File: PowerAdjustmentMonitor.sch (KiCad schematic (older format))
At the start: 19 parts

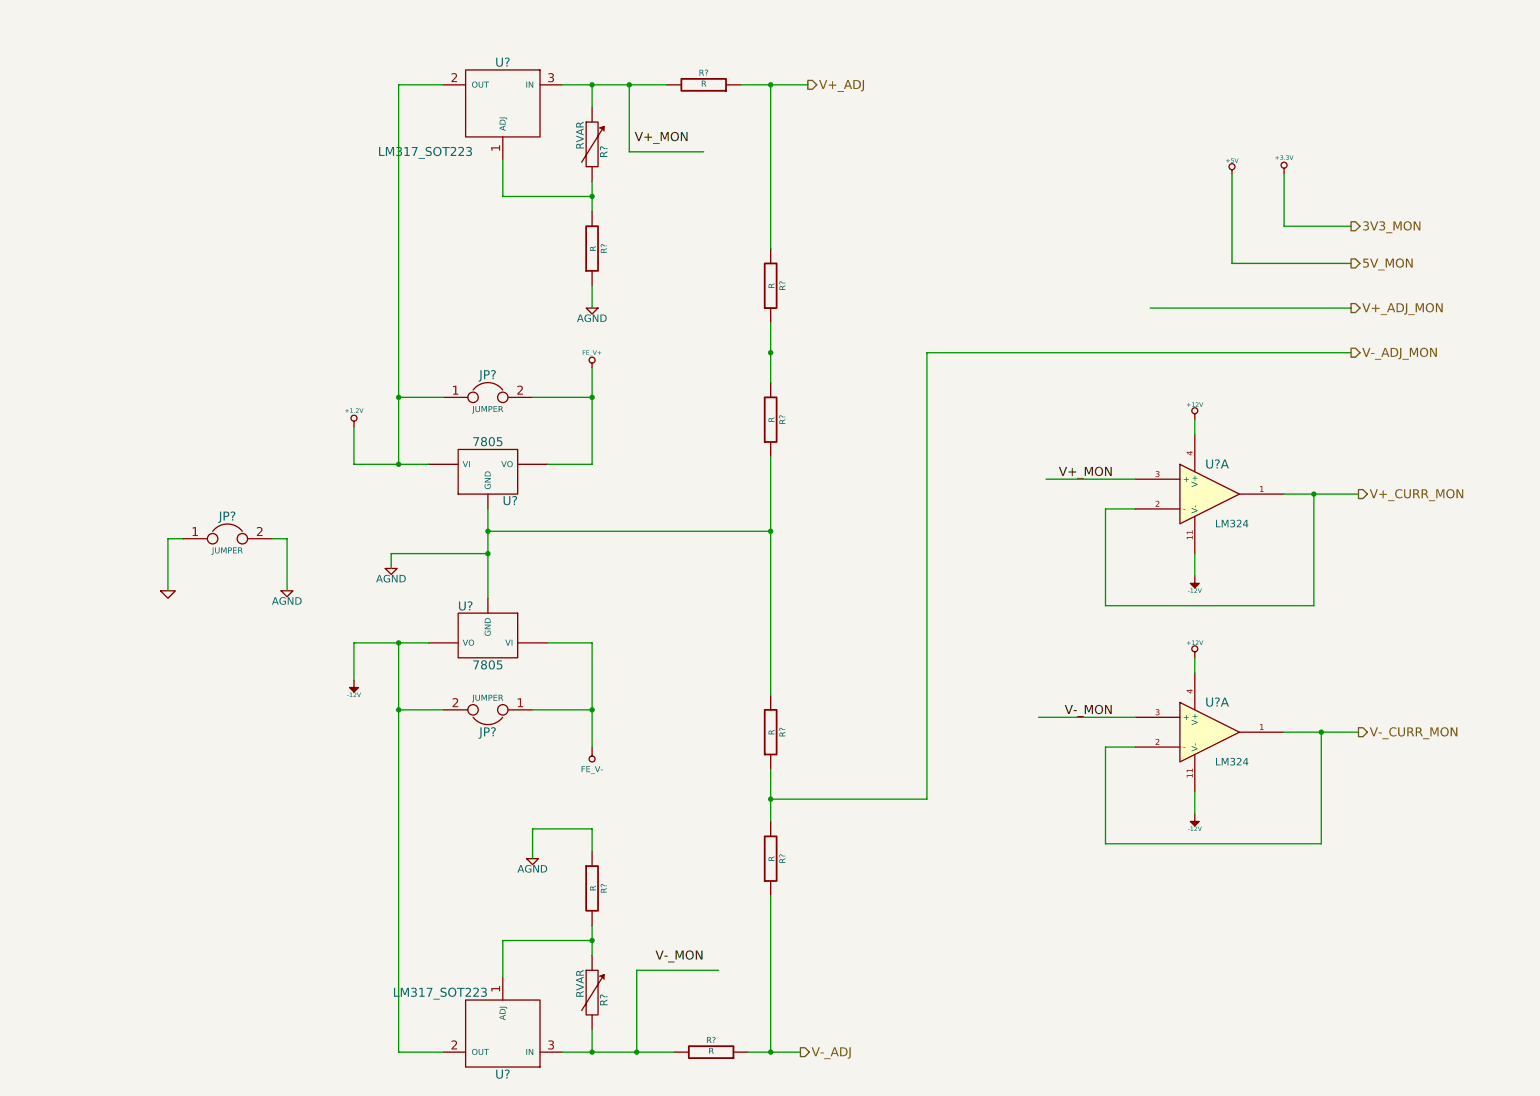
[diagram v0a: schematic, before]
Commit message: Added Relay module footprints.
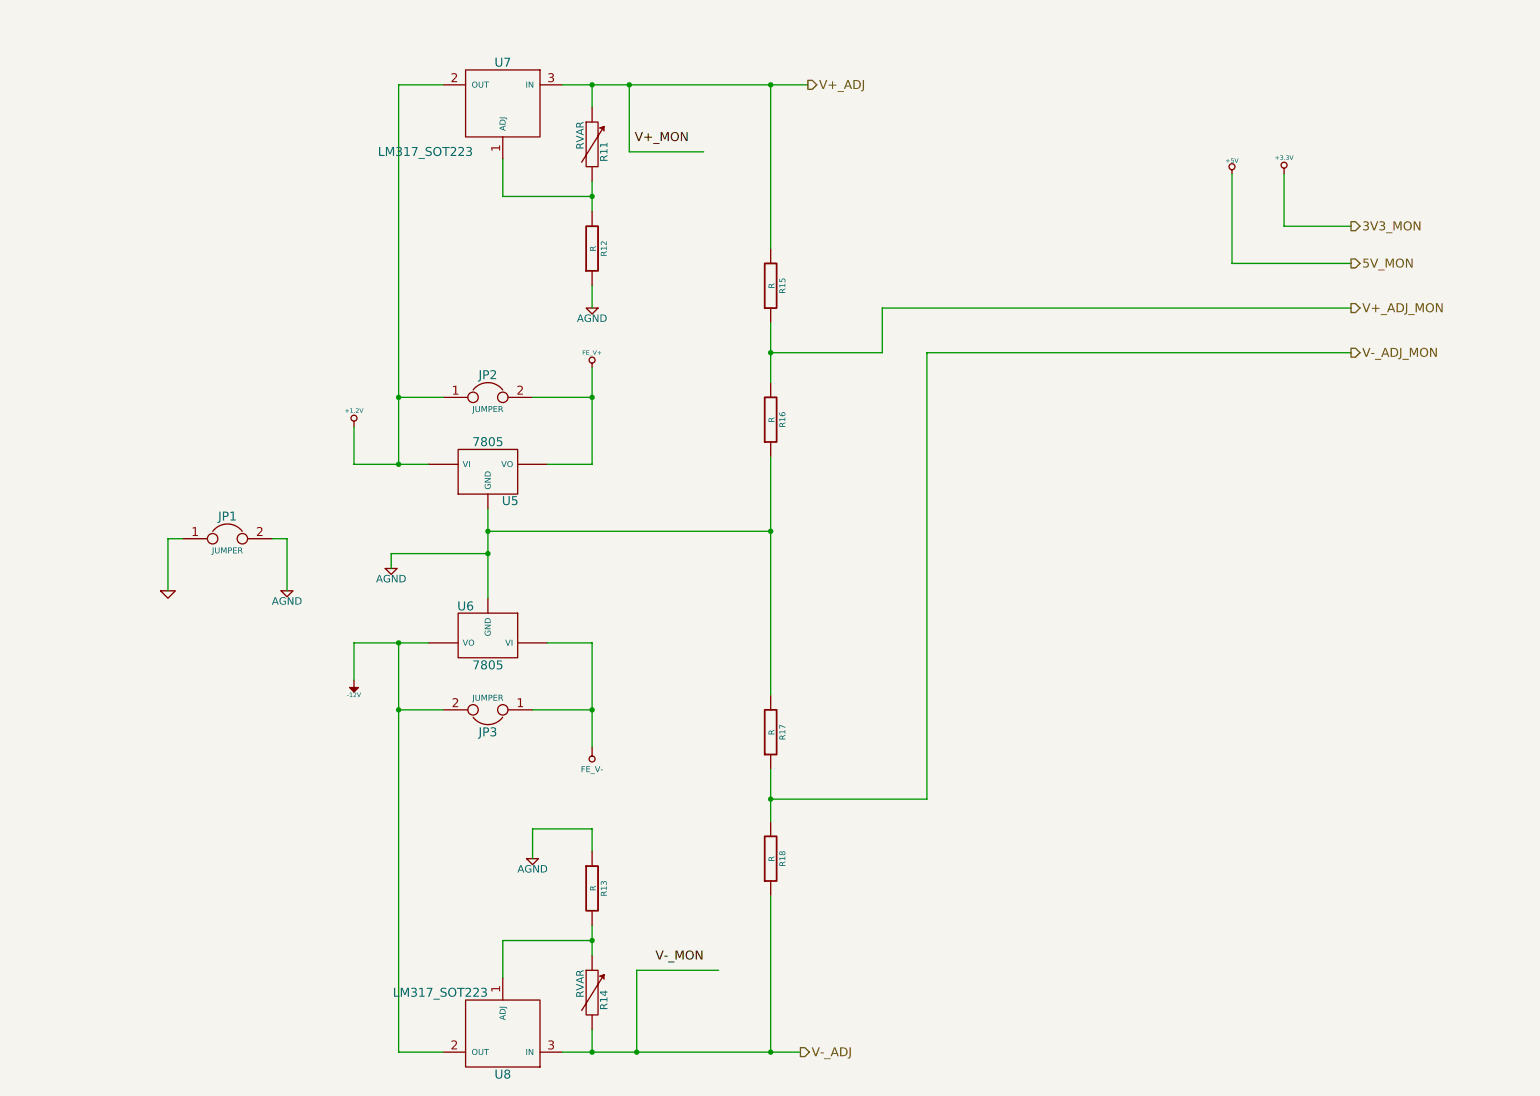
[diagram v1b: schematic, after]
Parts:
- removed R? (x2): R, symbol R
- removed U? (x2): LM324, symbol LM324
- gave numbers to parts that had none: 15
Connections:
- net labels removed: +12V, V+_CURR_MON, V-_CURR_MON
- wire segments 94 -> 57

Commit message: Associated and placed thermocouple, terminal, arduino, fan driver, power protection modules.
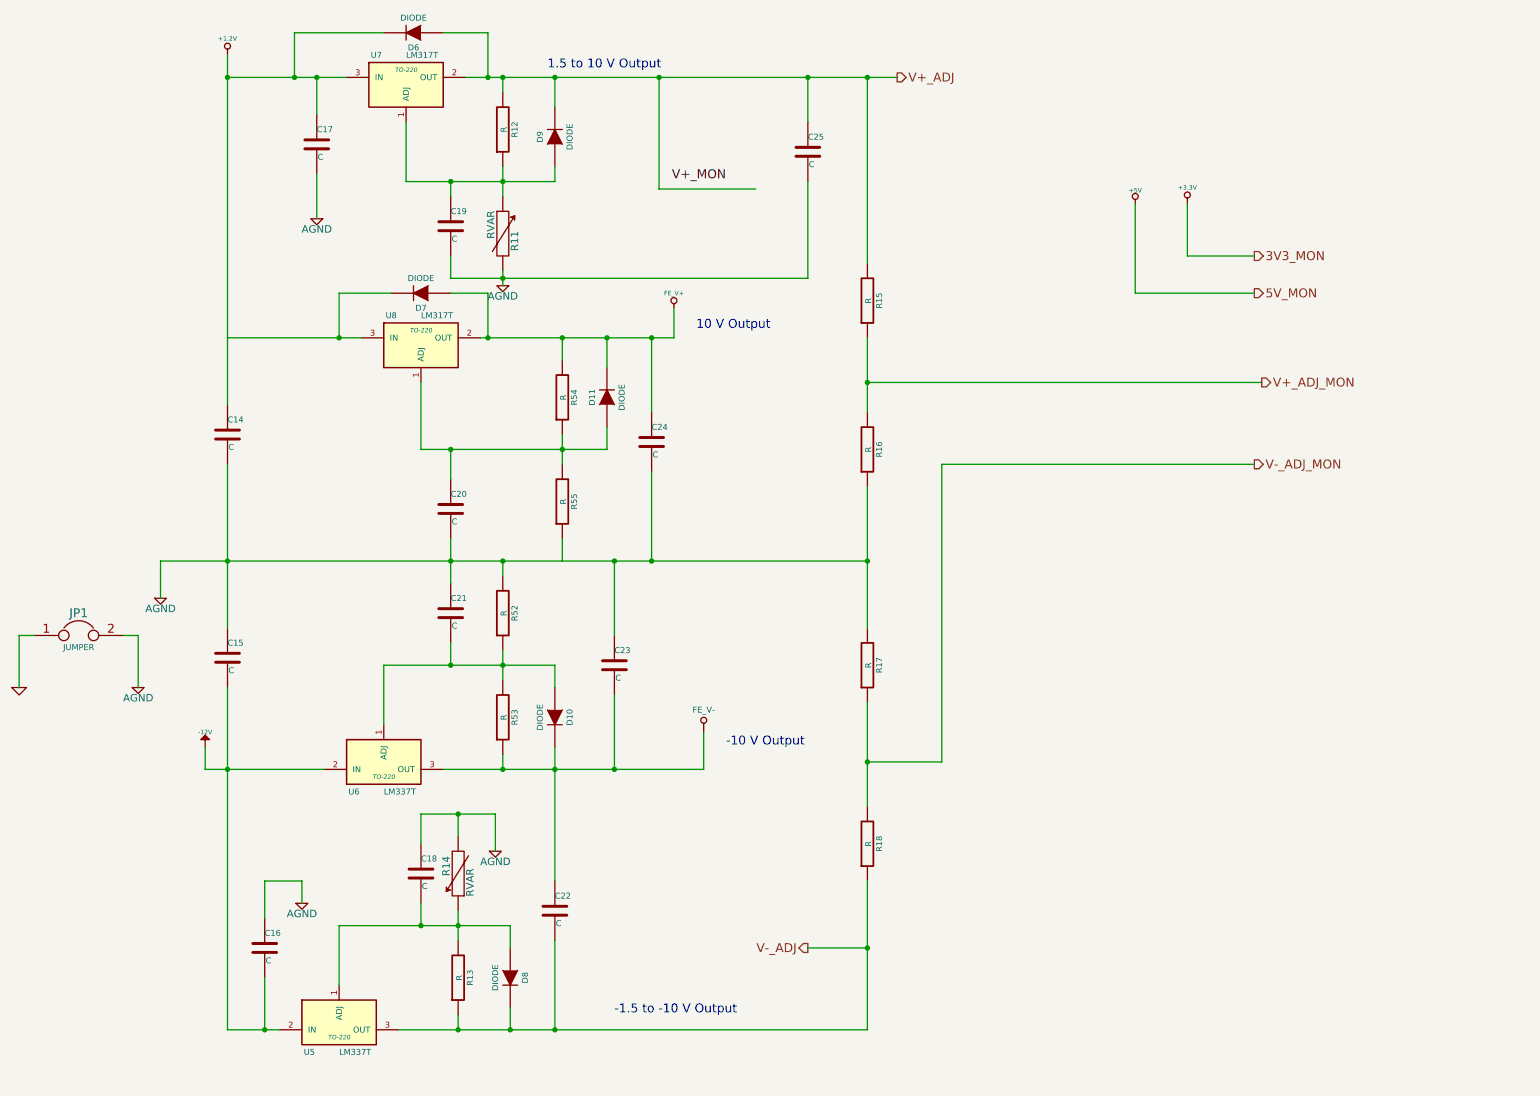
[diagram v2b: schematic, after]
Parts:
- removed JP2, JP3: JUMPER, symbol JUMPER
- removed U5, U6: 7805, symbol 7805
- removed U7, U8: LM317_SOT223, symbol LM317_SOT223
- added C14, C15, C16, C17, C18, C19, C20, C21, C22, C23, C24, C25: C, symbol C
- added D10, D11, D6, D7, D8, D9: DIODE, symbol DIODE
- added R52, R53, R54, R55: R, symbol R
- added U5, U6: LM337T, TO-220, symbol LM337T
- added U7, U8: LM317T, TO-220, symbol LM317T
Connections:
- net labels removed: V-_MON
- wire segments 57 -> 95
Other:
- note added: "-1.5 to -10 V Output"
- note added: "-10 V Output"
- note added: "1.5 to 10 V Output"
- note added: "10 V Output"
- moved on the sheet: JP1, R11, R12, R15, R16, R17, R18

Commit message: Layout sessions 1-4.
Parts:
- removed JP1: JUMPER, symbol JUMPER
- removed U7, U8: LM317T, TO-220, symbol LM317T
- added D12, D13: MMBD914-7-F, symbol DIODE
- added U7, U8: LM317_BB, TO-220, symbol LM317_BB
- D10, D11, D6, D7, D8: value DIODE -> MMBD914-7-F; MFG Part Number (none) -> MMBD914-7-F; MFG name (none) -> Diodes Inc
- D9: value DIODE -> MMBD914-7-F; MFG Part Number (none) -> MMBD914-7-F; MFG name (none) -> DiodeS Inc
- R11, R14: value RVAR -> 5K
- R12, R13: value R -> 715
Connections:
- net +1.2V: now also U7.2 (IN)
- net -12V: now also D12.2 (K), D13.2 (K)
- net AGND: now also D10.2 (K), R55.1; no longer C16.1, C17.2, C18.1, C19.2, C25.2, R11.2, R14.2, R16.1, R17.2
- net FE_V+: now also U8.3 (OUT)
- net FE_V-: now also D13.1 (A); no longer C22.1, D10.2 (K)
- net V+_ADJ: now also U7.3 (OUT)
- net V-_ADJ: now also D8.1 (A), D12.1 (A); no longer D8.2 (K)
- net at C19.1, D9.1 (A), R11.1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: now also U7.1 (ADJ)
- net at C20.1, D11.1 (A), R54.1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: now also U8.1 (ADJ)
- net at D7.2 (K): now also U8.2 (IN)
- net at C18.2, R13.2, R14.1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: now also D8.2 (K); no longer D8.1 (A)
- new net GND_PWR: C16.1, C17.2, C18.1, C19.2, C22.1, C25.2, R11.2, R14.2, R16.1, R17.2
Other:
- moved on the sheet: C14, C15, C16, C17, C18, C19, C20, C21, C22, C23, C24, C25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
